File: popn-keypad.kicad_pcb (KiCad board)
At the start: 2 copper layers, 130.9 x 40.5 mm, 14 parts, among them U1 Arduino_Pro_Micro

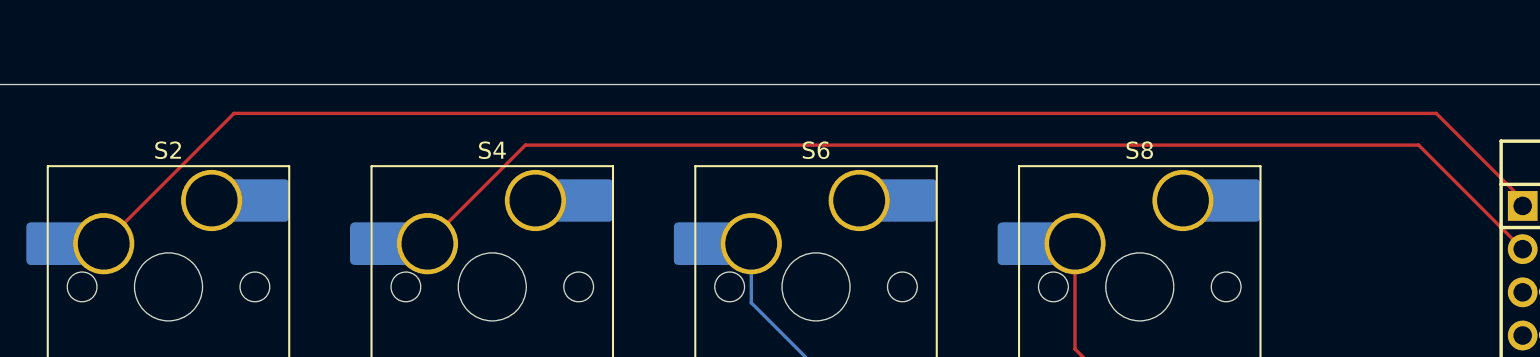
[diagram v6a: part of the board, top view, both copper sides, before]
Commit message: quick fix
Fixed warnings that came up as a result of the previous commit
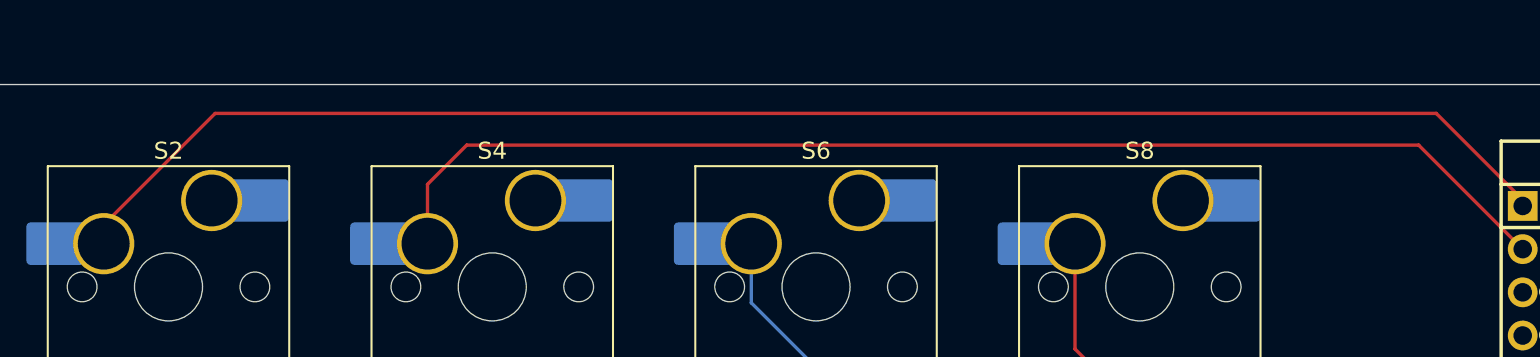
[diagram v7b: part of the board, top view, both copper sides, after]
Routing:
- net S2: track 69.4 -> 71.4 mm
- net S1: track 89.1 -> 89.7 mm
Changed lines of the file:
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@@
 	(segment
 		(start 115.51 73.62)
-		(end 123.172796 65.957204)
+		(end 115.51 72.51)
+		(width 0.2)
+		(layer "F.Cu")
+		(net 2)
+	)
+	(segment
+		(start 115.51 72.51)
+		(end 122.062796 65.957204)
+		(width 0.2)
+		(layer "F.Cu")
+		(net 2)
+	)
+	(segment
+		(start 193.876204 65.957204)
+		(end 198.96 71.041)
+		(width 0.2)
+		(layer "F.Cu")
+		(net 2)
+	)
+	(segment
+		(start 122.062796 65.957204)
+		(end 193.876204 65.957204)
 		(width 0.2)
 		(layer "F.Cu")
@@
 		(start 198.96 71.041)
 		(end 198.96 71.4)
-		(width 0.2)
-		(layer "F.Cu")
-		(net 2)
-	)
-	(segment
-		(start 123.172796 65.957204)
-		(end 193.876204 65.957204)
-		(width 0.2)
-		(layer "F.Cu")
-		(net 2)
-	)
-	(segment
-		(start 193.876204 65.957204)
-		(end 198.96 71.041)
 		(width 0.2)
 		(layer "F.Cu")
@@
 	)
 	(segment
-		(start 134.55 73.62)
-		(end 134.55 73.581484)
-		(width 0.2)
-		(layer "F.Cu")
-		(net 7)
-	)
-	(segment
-		(start 134.55 73.581484)
-		(end 140.30844 67.823044)
-		(width 0.2)
-		(layer "F.Cu")
-		(net 7)
-	)
-	(segment
-		(start 140.30844 67.823044)
+		(start 136.856956 67.823044)
 		(end 192.843044 67.823044)
 		(width 0.2)
@@
 		(width 0.2)
 		(layer "F.Cu")
+		(net 7)
+	)
+	(segment
+		(start 134.55 73.62)
+		(end 134.55 70.13)
+		(width 0.2)
+		(layer "F.Cu")
+		(net 7)
+	)
+	(segment
+		(start 134.55 70.13)
+		(end 136.856956 67.823044)
+		(width 0.2)
+		(layer "F.Cu")

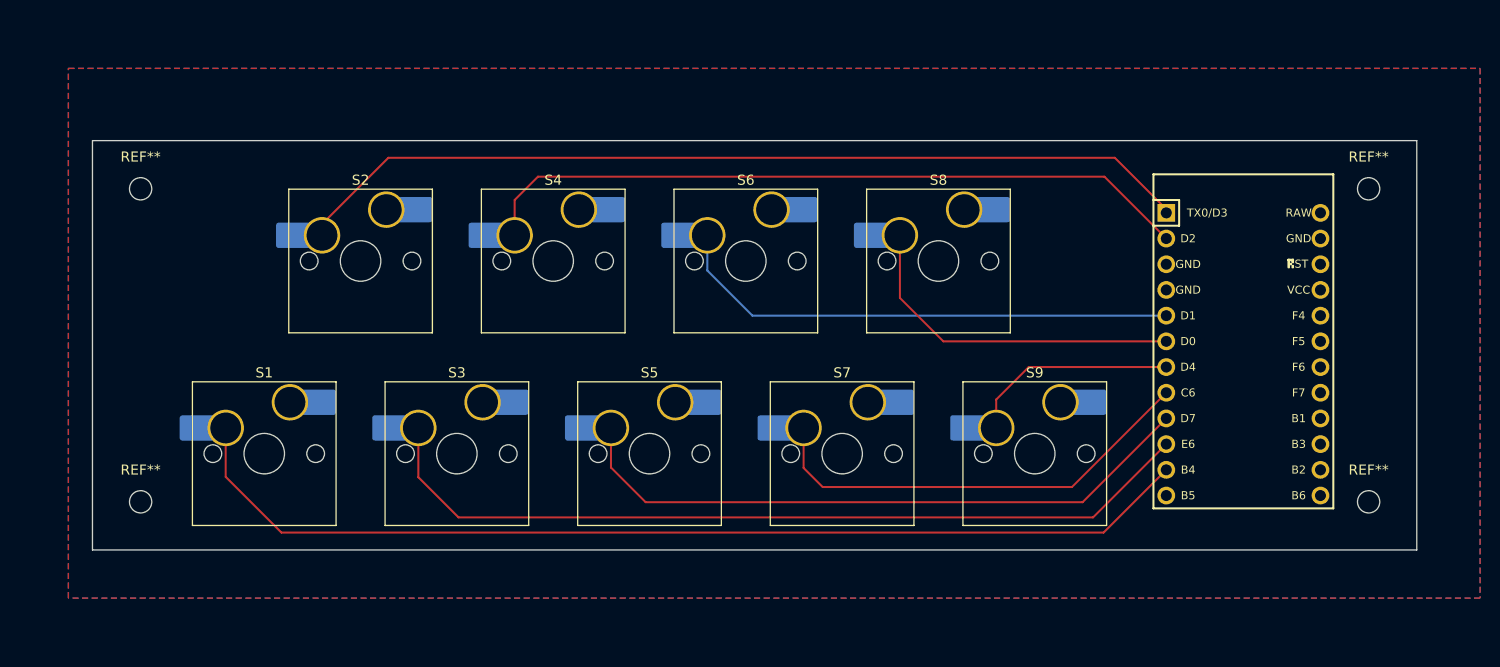
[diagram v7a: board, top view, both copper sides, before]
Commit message: Adjusted keypad dimensions
Made the keypad wider, to better accommodate for the mount holes and the case
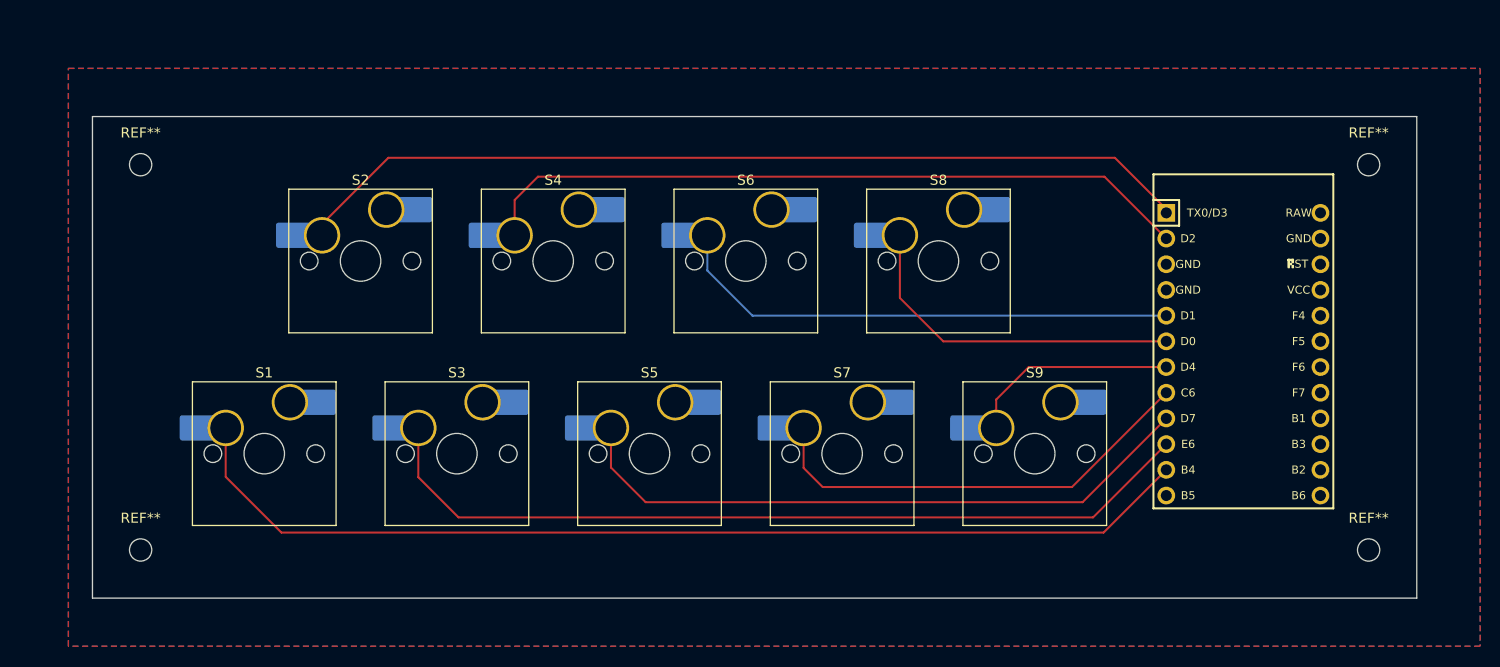
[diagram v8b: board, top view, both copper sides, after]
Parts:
- moved REF** 4.76 mm to (97.6, 104.7)
- moved REF** 4.76 mm to (219.0, 104.7)
- moved REF** 2.38 mm to (219.0, 66.6)
- moved REF** 2.38 mm to (97.6, 66.6)
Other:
- board size 130.9 x 40.5 mm -> 130.9 x 47.6 mm
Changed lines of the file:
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@@
 	(footprint "MountingHole:MountingHole_2.2mm_M2"
 		(layer "F.Cu")
-		(at 97.58 99.96)
+		(at 97.58 104.72)
 		(descr "Mounting Hole 2.2mm, M2, no annular, generated by kicad-footprint-generator mountinghole.py")
 		(tags "mountinghole M2")
@@
 	(footprint "MountingHole:MountingHole_2.2mm_M2"
 		(layer "F.Cu")
-		(at 218.96 69.02)
+		(at 218.96 66.64)
 		(descr "Mounting Hole 2.2mm, M2, no annular, generated by kicad-footprint-generator mountinghole.py")
 		(tags "mountinghole M2")
@@
 	(footprint "MountingHole:MountingHole_2.2mm_M2"
 		(layer "F.Cu")
-		(at 218.96 99.96)
+		(at 218.96 104.72)
 		(descr "Mounting Hole 2.2mm, M2, no annular, generated by kicad-footprint-generator mountinghole.py")
 		(tags "mountinghole M2")
@@
 	(footprint "MountingHole:MountingHole_2.2mm_M2"
 		(layer "F.Cu")
-		(at 97.58 69.02)
+		(at 97.58 66.64)
 		(descr "Mounting Hole 2.2mm, M2, no annular, generated by kicad-footprint-generator mountinghole.py")
 		(tags "mountinghole M2")
@@
 	)
 	(gr_rect
-		(start 92.82 64.26)
-		(end 223.72 104.72)
+		(start 92.82 61.88)
+		(end 223.72 109.48)
 		(stroke
 			(width 0.05)
@@
 		(polygon
 			(pts
-				(xy 90.44 57.12) (xy 229.98 57.12) (xy 229.98 109.48) (xy 90.44 109.48)
+				(xy 90.44 57.12) (xy 229.98 57.12) (xy 229.98 114.24) (xy 90.44 114.24)
 			)
 		)
